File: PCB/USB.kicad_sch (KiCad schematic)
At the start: 7 parts, among them U20 xc7z020clg484

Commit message: [+] routing done, need to fix minor errors.
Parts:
- gave numbers to parts that had none: 4
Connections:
- net JOYMISO: now also U20.C8 (PS_MIO41_501); no longer U20.A11 (PS_MIO30_501)
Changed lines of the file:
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@@
-	)
-	(no_connect
-		(at 125.095 125.73)
 	)
 	(no_connect
@@
 	(no_connect
 		(at 125.095 153.67)
+	)
+	(no_connect
+		(at 125.095 97.79)
 	)
 	(no_connect
@@
 		)
 	)
+	(global_label "JOYMISO"
+		(shape output)
+		(at 125.095 125.73 180)
+		(fields_autoplaced yes)
+		(effects
+			(font
+				(size 1.27 1.27)
+			)
+			(justify right)
+		)
+		(property "Intersheetrefs" "${INTERSHEET_REFS}"
+			(at 114.7811 125.73 0)
+			(effects
+				(font
+					(size 1.27 1.27)
+				)
+				(justify right)
+				(hide yes)
+			)
+		)
+	)
 	(global_label "JOYSCK"
 		(shape output)
@@
 					(size 1.27 1.27)
 				)
-				(hide yes)
-			)
-		)
-	)
-	(global_label "JOYMISO"
-		(shape output)
-		(at 125.095 97.79 180)
-		(fields_autoplaced yes)
-		(effects
-			(font
-				(size 1.27 1.27)
-			)
-			(justify right)
-		)
-		(property "Intersheetrefs" "${INTERSHEET_REFS}"
-			(at 114.7811 97.79 0)
-			(effects
-				(font
-					(size 1.27 1.27)
-				)
-				(justify right)
 				(hide yes)
 			)
@@
 					(unit 1)
 				)
-				(path "/0cf42e13-7c72-4f5f-898b-a3f851b94890/00000000-0000-0000-0000-00005852ff3b"
-					(reference "R?")
-					(unit 1)
-				)
 			)
 		)
@@
 		(on_board yes)
 		(dnp no)
-		(property "Reference" "C?"
+		(property "Reference" "C67"
 			(at 118.999 164.592 0)
 			(effects
@@
 		(instances
 			(project "DFTBoard"
-				(path "/0cf42e13-7c72-4f5f-898b-a3f851b94890/00000000-0000-0000-0000-000058508414"
-					(reference "C?")
-					(unit 1)
-				)
 				(path "/0cf42e13-7c72-4f5f-898b-a3f851b94890/00000000-0000-0000-0000-00005852a88e"
 					(reference "C67")
@@
 		(on_board yes)
 		(dnp no)
-		(property "Reference" "C?"
+		(property "Reference" "C65"
 			(at 106.299 164.592 0)
 			(effects
@@
 		(instances
 			(project "DFTBoard"
-				(path "/0cf42e13-7c72-4f5f-898b-a3f851b94890/00000000-0000-0000-0000-000058508414"
-					(reference "C?")
-					(unit 1)
-				)
 				(path "/0cf42e13-7c72-4f5f-898b-a3f851b94890/00000000-0000-0000-0000-00005852a88e"
 					(reference "C65")
@@
 		(on_board yes)
 		(dnp no)
-		(property "Reference" "C?"
+		(property "Reference" "C66"
 			(at 112.649 164.592 0)
 			(effects
@@
 		(instances
 			(project "DFTBoard"
-				(path "/0cf42e13-7c72-4f5f-898b-a3f851b94890/00000000-0000-0000-0000-000058508414"
-					(reference "C?")
-					(unit 1)
-				)
 				(path "/0cf42e13-7c72-4f5f-898b-a3f851b94890/00000000-0000-0000-0000-00005852a88e"
 					(reference "C66")
@@
 		(on_board yes)
 		(dnp no)
-		(property "Reference" "#PWR?"
+		(property "Reference" "#PWR0102"
 			(at 112.395 171.45 0)
 			(effects
@@
 		(instances
 			(project "DFTBoard"
-				(path "/0cf42e13-7c72-4f5f-898b-a3f851b94890/00000000-0000-0000-0000-000058508414"
-					(reference "#PWR?")
-					(unit 1)
-				)
 				(path "/0cf42e13-7c72-4f5f-898b-a3f851b94890/00000000-0000-0000-0000-00005852a88e"
 					(reference "#PWR0102")
@@
 		(on_board yes)
 		(dnp no)
-		(property "Reference" "R?"
+		(property "Reference" "R26"
 			(at 122.555 57.2516 90)
 			(effects
@@
 		(instances
 			(project "DFTBoard"
-				(path "/0cf42e13-7c72-4f5f-898b-a3f851b94890/00000000-0000-0000-0000-000058508444"
-					(reference "R?")
-					(unit 1)
-				)
 				(path "/0cf42e13-7c72-4f5f-898b-a3f851b94890/00000000-0000-0000-0000-00005852a88e"
 					(reference "R26")

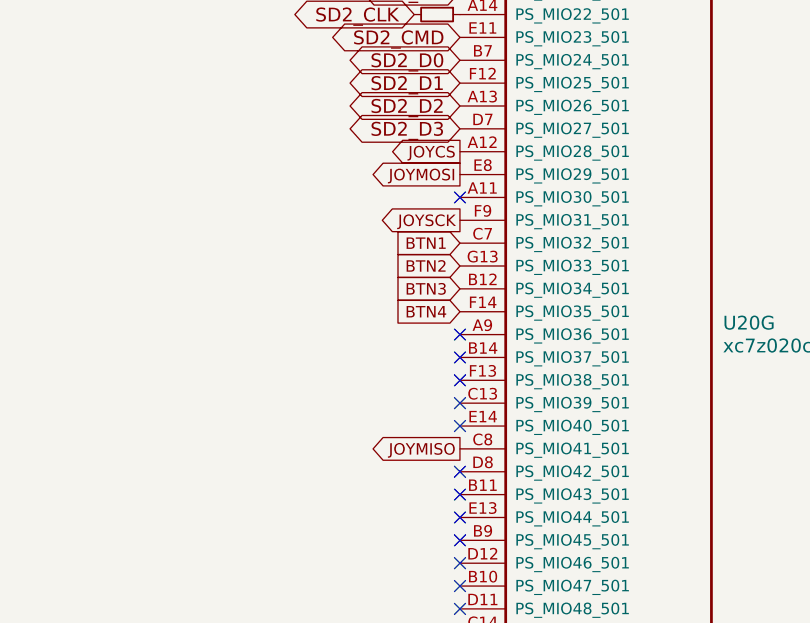
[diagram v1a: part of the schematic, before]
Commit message: Resolved most of the errors
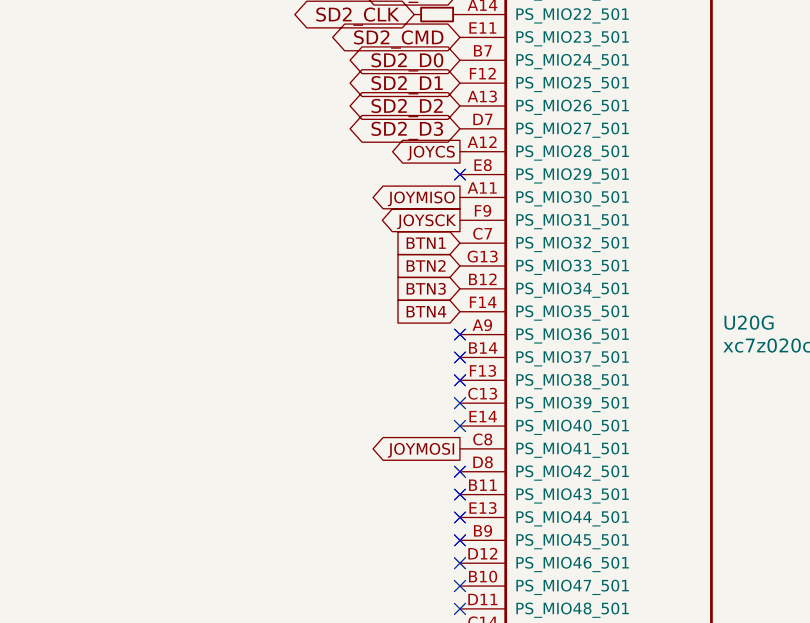
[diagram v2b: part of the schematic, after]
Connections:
- net JOYMISO: now also U20.A11 (PS_MIO30_501); no longer U20.C8 (PS_MIO41_501)
- net JOYMOSI: now also U20.C8 (PS_MIO41_501); no longer U20.E8 (PS_MIO29_501)
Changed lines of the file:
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@@
+	)
+	(no_connect
+		(at 125.095 95.25)
 	)
 	(no_connect
@@
 	(no_connect
 		(at 125.095 153.67)
-	)
-	(no_connect
-		(at 125.095 97.79)
 	)
 	(no_connect
@@
 		)
 	)
+	(global_label "JOYMISO"
+		(shape output)
+		(at 125.095 97.79 180)
+		(fields_autoplaced yes)
+		(effects
+			(font
+				(size 1.27 1.27)
+			)
+			(justify right)
+		)
+		(property "Intersheetrefs" "${INTERSHEET_REFS}"
+			(at 114.7811 97.79 0)
+			(effects
+				(font
+					(size 1.27 1.27)
+				)
+				(justify right)
+				(hide yes)
+			)
+		)
+	)
 	(global_label "SD2_CMD"
 		(shape bidirectional)
@@
 		)
 	)
-	(global_label "JOYMISO"
-		(shape output)
-		(at 125.095 125.73 180)
-		(fields_autoplaced yes)
-		(effects
-			(font
-				(size 1.27 1.27)
-			)
-			(justify right)
-		)
-		(property "Intersheetrefs" "${INTERSHEET_REFS}"
-			(at 114.7811 125.73 0)
-			(effects
-				(font
-					(size 1.27 1.27)
-				)
-				(justify right)
-				(hide yes)
-			)
-		)
-	)
 	(global_label "JOYSCK"
 		(shape output)
@@
 	(global_label "JOYMOSI"
 		(shape output)
-		(at 125.095 95.25 180)
-		(fields_autoplaced yes)
-		(effects
-			(font
-				(size 1.27 1.27)
-			)
-			(justify right)
-		)
-		(property "Intersheetrefs" "${INTERSHEET_REFS}"
-			(at 114.7811 95.25 0)
-			(effects
-				(font
+		(at 125.095 125.73 180)
+		(fields_autoplaced yes)
+		(effects
+			(font
+				(size 1.27 1.27)
+			)
+			(justify right)
+		)
+		(property "Intersheetrefs" "${INTERSHEET_REFS}"
+			(at 114.7811 125.73 0)
+			(effects
+				(font
